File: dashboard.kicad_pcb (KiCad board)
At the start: 2 copper layers, 87.6 x 57.2 mm, 27 parts, among them J1 Conn_01x06, J2 Conn_01x04, J3 RJ45, J4 ESTOP, J5 776267-1, U1 MCP2515-xSO, U2 MCP2551-I-P, U3 LM317_SOT-223, U4 ILD74, Y1 16M

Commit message: Route PCB
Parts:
- removed A1: Arduino_Nano_v2.x, FBR_Footprints:Arduino_Nano_3D
- removed C1, C2: 27p, Capacitor_THT:C_Disc_D5.1mm_W3.2mm_P5.00mm
- removed C3: 0.1u, Capacitor_SMD:C_0603_1608Metric_Pad1.08x0.95mm_HandSolder
- removed C4: 1u, Capacitor_SMD:C_0603_1608Metric_Pad1.08x0.95mm_HandSolder
- removed J1: Conn_01x06, Connector_PinHeader_2.54mm:PinHeader_1x06_P2.54mm_Vertical
- removed R2: 20k, Resistor_THT:R_Axial_DIN0207_L6.3mm_D2.5mm_P7.62mm_Horizontal
- removed R3: 715, Resistor_SMD:R_0603_1608Metric_Pad0.98x0.95mm_HandSolder
- removed R4: 240, Resistor_SMD:R_0603_1608Metric_Pad0.98x0.95mm_HandSolder
- removed U1: MCP2515-xSO, Package_DIP:DIP-18_W7.62mm
- removed U3: LM317_SOT-223, Package_TO_SOT_SMD:SOT-223-3_TabPin2
- removed Y1: 16M, Crystal:Crystal_HC49-U_Vertical
- added C8: 10u, Capacitor_THT:C_Disc_D5.1mm_W3.2mm_P5.00mm, F.Cu at (122.5, 101.0)
- added C9: 10u, Capacitor_THT:C_Disc_D5.1mm_W3.2mm_P5.00mm, F.Cu at (108.5, 101.0)
- added L3: 12u, Inductor_SMD:L_Wuerth_WE-PD-Typ-7345, F.Cu at (115.5, 103.5)
- added Q1: 2N7002, Package_TO_SOT_THT:TO-92L_Inline_Wide, F.Cu at (116.5, 132.2)
- J2: value Conn_01x04 -> Conn_01x02; footprint Connector_PinHeader_2.54mm:PinHeader_1x04_P2.54mm_Vertical -> Connector_JST:JST_EH_B2B-EH-A_1x02_P2.50mm_Vertical
- J4: value ESTOP -> Conn_01x10; footprint Connector_PinHeader_2.54mm:PinHeader_1x02_P2.54mm_Vertical -> Connector_JST:JST_EH_B10B-EH-A_1x10_P2.50mm_Vertical
- R1: value 10k -> 120
- R6, R7: footprint Resistor_SMD:R_0603_1608Metric_Pad0.98x0.95mm_HandSolder -> Resistor_THT:R_Axial_DIN0207_L6.3mm_D2.5mm_P7.62mm_Horizontal
- U2: value MCP2551-I-P -> R-78C5.0-1.0; footprint Package_DIP:DIP-8_W7.62mm -> Converter_DCDC:Converter_DCDC_RECOM_R-78E-0.5_THT
- moved J4 81.4 mm to (180.5, 124.8), turned to 90 degrees
- moved U2 44.1 mm to (113.0, 96.5)
- moved R5 26.1 mm to (174.5, 123.2)
- moved U4 21.9 mm to (130.1, 138.5), turned to 180 degrees
- moved R6 19.3 mm to (122.5, 121.9)
- moved R7 18.2 mm to (122.5, 126.4)
- moved R1 14.1 mm to (110.4, 138.6), turned to 0 degrees
- moved J2 5.61 mm to (103.0, 112.5), turned to -90 degrees
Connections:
- J2 pad 1: +5V -> /Shutdown1
- J2 pad 2: /DISP_TX -> /Shutdown2
- J3 pad 2: +12V -> +5V
- J4 pad 1: /Shutdown1 -> /Neutral_LED+
- J4 pad 2: /Shutdown2 -> /Neutral
- J5 pad 12: GND -> /Spare_Switch_Sig
- U2 pad 1: /CAN_TX -> Net-(U2-IN)
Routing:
- net /SPI_CS: track 55.7 -> 0.00 mm
- net /SPI_MISO: track 53.7 -> 0.00 mm
- net +5V: track 187.4 -> 135.6 mm, vias 1 -> 0
- net /SPI_SCK: track 50.9 -> 0.00 mm, vias 1 -> 0
- net /SPI_MOSI: track 50.3 -> 0.00 mm
- net /Shift_Up: track 80.2 -> 44.0 mm
- net /Shutdown2: track 55.8 -> 91.1 mm, vias 0 -> 1
- net /Spare_Switch_Sig: track 0.00 -> 34.0 mm
- net /Shift_Dn: track 76.0 -> 42.2 mm
- net /CANH: track 61.8 -> 30.4 mm
- net /Shutdown1: track 51.1 -> 81.7 mm, vias 0 -> 1
- net /CANL: track 56.1 -> 28.9 mm
- net /DISP_TX: track 22.1 -> 0.00 mm
- net /DISP_RX: track 22.1 -> 0.00 mm
- net /CAN_TX: track 15.7 -> 0.00 mm
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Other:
- board text added: "+"
- board text added: "-"
- board text added: "Fan SW"
- board text added: "Neutral"
- board text added: "SW2"
- board text added: "Shtdwn"
- board text added: "Starter"
- board text removed: "5V"
- board text removed: "ESTOP"
- board text removed: "Fan SW - +"
- board text removed: "GND"
- board text removed: "Neutral - +"
- board text removed: "RX"
- board text removed: "Starter - +"
- board text removed: "TX"

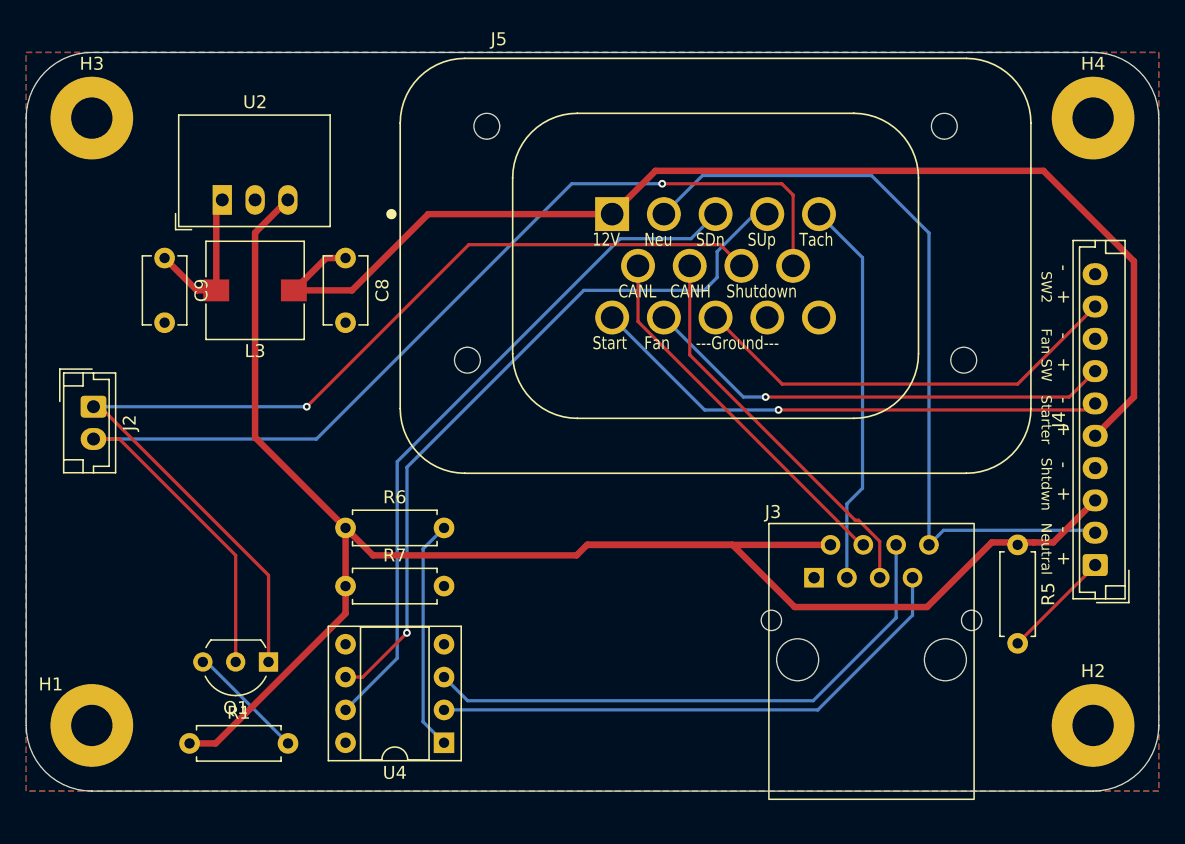
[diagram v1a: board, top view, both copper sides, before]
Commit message: Add both power supplies
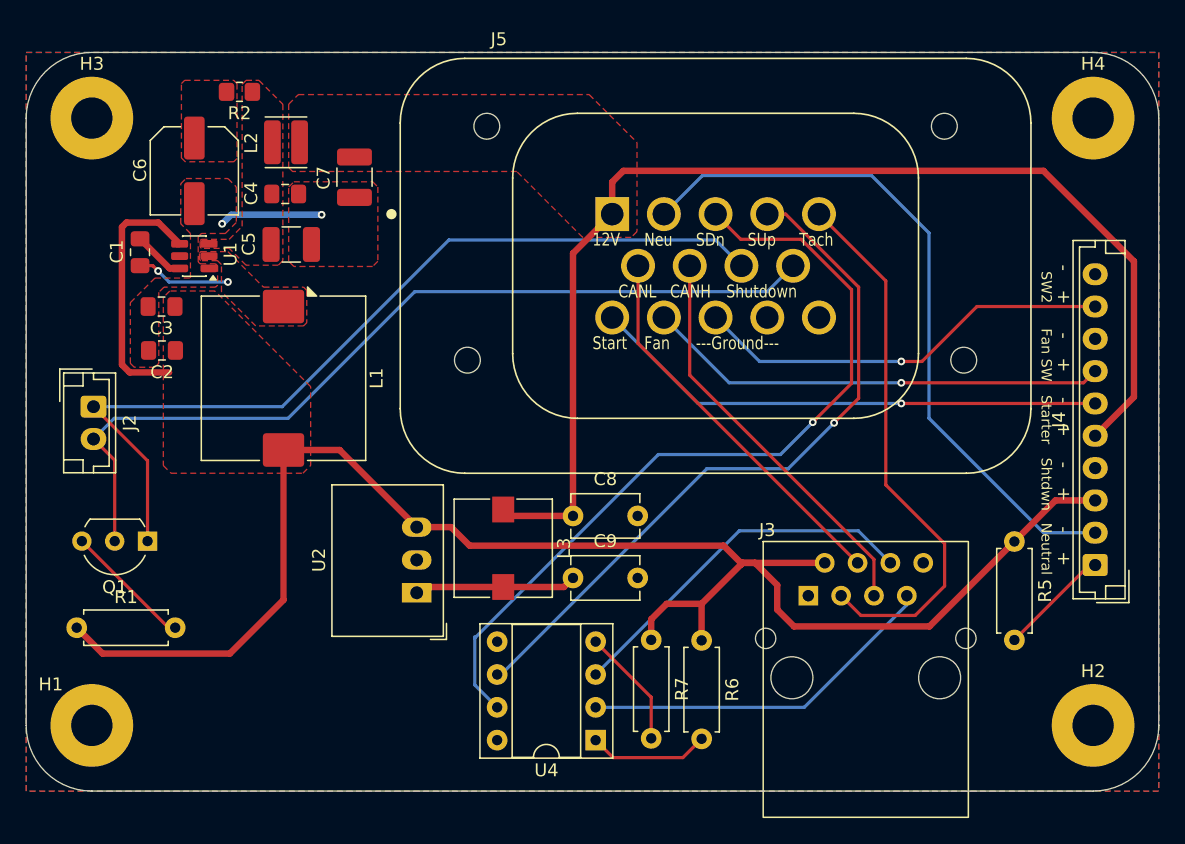
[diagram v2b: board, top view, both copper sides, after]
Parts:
- added C1: 100n, Capacitor_SMD:C_0805_2012Metric_Pad1.18x1.45mm_HandSolder, F.Cu at (106.6, 100.5)
- added C2: 22u, Capacitor_SMD:C_0805_2012Metric_Pad1.18x1.45mm_HandSolder, F.Cu at (108.3, 108.2)
- added C3: 100n, Capacitor_SMD:C_0805_2012Metric_Pad1.18x1.45mm_HandSolder, F.Cu at (108.3, 104.8)
- added C4: 100n, Capacitor_SMD:C_0805_2012Metric_Pad1.18x1.45mm_HandSolder, F.Cu at (117.8, 96.0)
- added C5: 22u, Capacitor_SMD:C_1210_3225Metric_Pad1.33x2.70mm_HandSolder, F.Cu at (118.3, 100.0)
- added C6: 56u, Capacitor_SMD:C_Elec_6.3x5.8, F.Cu at (110.8, 94.2)
- added C7: 10u, Capacitor_SMD:C_1210_3225Metric_Pad1.33x2.70mm_HandSolder, F.Cu at (123.2, 94.7)
- added L1: 15u, Inductor_SMD:L_TDK_SLF12575, F.Cu at (117.7, 110.3)
- added L2: 560n, Inductor_SMD:L_Wuerth_MAPI-3012, F.Cu at (117.9, 92.0)
- added R2: 100m, Resistor_SMD:R_0805_2012Metric_Pad1.20x1.40mm_HandSolder, F.Cu at (114.3, 88.1)
- added U1: TPS542025DDC, Package_TO_SOT_SMD:SOT-23-6, F.Cu at (110.8, 100.8)
- moved C9 40.1 mm to (140.1, 125.8), turned to 0 degrees
- moved U2 33.9 mm to (128.0, 126.9), turned to 90 degrees
- moved R6 28.9 mm to (150.1, 130.6), turned to -90 degrees
- moved L3 27.7 mm to (134.7, 123.5), turned to -90 degrees
- moved C8 26.6 mm to (140.1, 121.0), turned to 0 degrees
- moved R7 24.0 mm to (146.2, 130.5), turned to -90 degrees
- moved Q1 13.2 mm to (107.2, 122.9)
- moved R1 12.5 mm to (101.7, 129.6)
- moved U4 11.7 mm to (141.8, 138.3)
- moved J3 1.46 mm to (158.3, 127.1)
- moved R5 0.36 mm to (174.2, 122.9)
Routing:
- net /Shutdown2: track 91.1 -> 69.0 mm, vias 1 -> 0
- net /Shift_Up: track 44.0 -> 28.4 mm
- net /Shift_Dn: track 42.2 -> 28.1 mm
- net /Shutdown1: track 81.7 -> 68.4 mm, vias 1 -> 0
- net /Tacho: track 30.0 -> 42.4 mm
- net /Shift_Dn_Out: track 53.4 -> 63.7 mm, vias 0 -> 1
- net Net-(R7-Pad2): track 0.00 -> 9.26 mm
- net Net-(R6-Pad2): track 18.0 -> 9.36 mm
- net +5V: track 135.6 -> 143.6 mm
- net GND: track 0.00 -> 7.99 mm, vias 0 -> 2
- net Net-(U1-SW): track 0.00 -> 7.32 mm, vias 0 -> 2
- net /Neutral: track 61.1 -> 54.4 mm
- net Net-(U1-BOOT): track 0.00 -> 4.01 mm
- net /Spare_Switch_Sig: track 34.0 -> 32.5 mm, vias 0 -> 1
- net /CANL: track 28.9 -> 30.0 mm
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- added copper zone on F.Cu, net +12V
- added copper zone on F.Cu, net +5V
- added copper zone on F.Cu, net Net-(C6-Pad1)
- added copper zone on F.Cu, net Net-(U1-SW)
- added copper zone on F.Cu, net Net-(U1-VIN)

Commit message: Add power supply protection
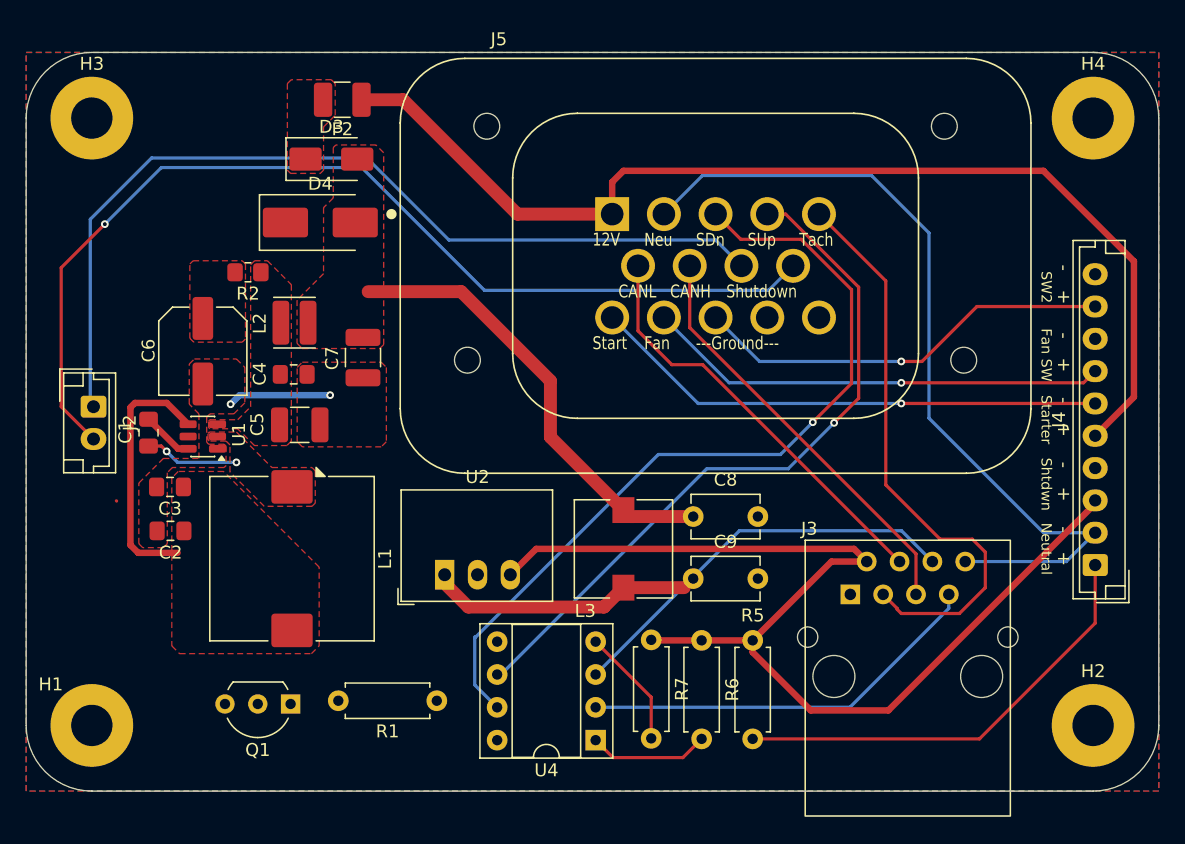
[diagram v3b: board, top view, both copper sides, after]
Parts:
- added D3: SS34, Diode_SMD:D_SMA, F.Cu at (121.4, 93.3)
- added D4: SMBJ24CA, Diode_SMD:D_SMB_Handsoldering, F.Cu at (120.5, 98.2)
- added F2: MF-USHTD75KX/24-2, Fuse:Fuse_1210_3225Metric_Pad1.42x2.65mm_HandSolder, F.Cu at (122.2, 88.8)
- moved R1 28.4 mm to (129.6, 135.2), turned to 180 degrees
- moved R5 21.6 mm to (154.0, 130.6)
- moved Q1 16.8 mm to (118.2, 135.5)
- moved C1 14.0 mm to (107.3, 114.5)
- moved C2 14.0 mm to (109.0, 122.1)
- moved C3 14.0 mm to (108.9, 118.7)
- moved C4 14.0 mm to (118.5, 110.0)
- moved C5 14.0 mm to (119.0, 113.9)
- moved C6 14.0 mm to (111.5, 108.2)
- moved C7 14.0 mm to (123.8, 108.7)
- moved L1 14.0 mm to (118.4, 124.3)
- moved L2 14.0 mm to (118.5, 106.0)
- moved R2 14.0 mm to (115.0, 102.1)
- moved U1 14.0 mm to (111.5, 114.8)
- moved C8 9.30 mm to (149.4, 121.0)
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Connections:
- C7 pad 1: +12V -> /PSU+
- C8 pad 1: +12V -> /PSU+
- L2 pad 1: +12V -> /PSU+
- L3 pad 1: +12V -> /PSU+
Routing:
- net +5V: track 143.6 -> 104.3 mm
- net /PSU+: track 0.00 -> 34.2 mm
- net /Neutral_LED+: track 8.65 -> 34.7 mm
- net /Neutral: track 54.4 -> 65.4 mm
- net /Shutdown2: track 69.0 -> 79.6 mm, vias 0 -> 1
- net Net-(Q1-D): track 10.00 -> 0.00 mm
- net Net-(U2-IN): track 12.9 -> 21.6 mm
- net +12V: track 91.1 -> 83.9 mm
- net /Shift_Dn: track 28.1 -> 31.6 mm
- net /Shift_Up: track 28.4 -> 31.6 mm
- net /Tacho: track 42.4 -> 45.1 mm
- net /CANL: track 30.0 -> 32.7 mm
- net /Shutdown1: track 68.4 -> 70.4 mm
- net /CANH: track 31.4 -> 32.7 mm
- added copper zone on F.Cu, net /PSU+
- added copper zone on F.Cu, net Net-(D3-K)
- removed copper zone on F.Cu, net +12V

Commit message: Revert "Add power supply protection"
This reverts commit 6c38df0548b9625adbd3b6c051cb9005b09ba150.
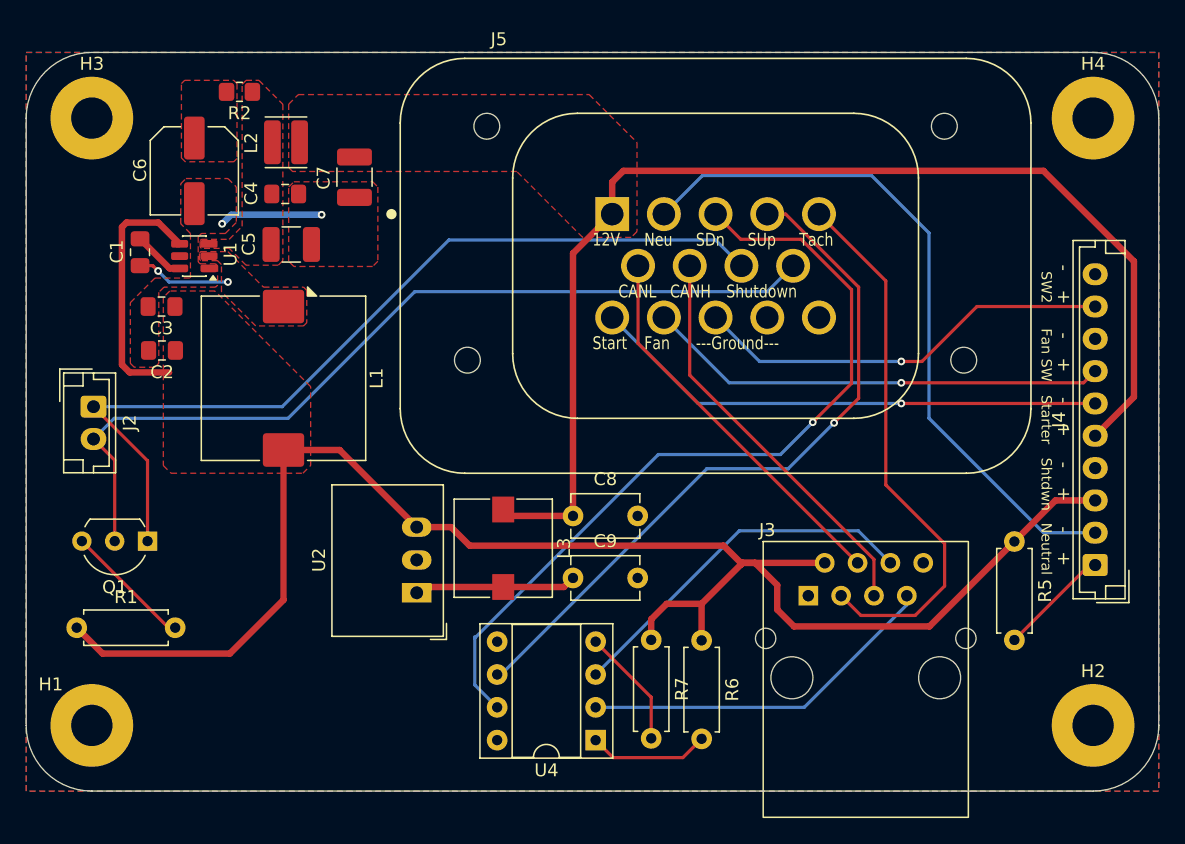
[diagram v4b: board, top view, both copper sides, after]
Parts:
- removed D3: SS34, Diode_SMD:D_SMA
- removed D4: SMBJ24CA, Diode_SMD:D_SMB_Handsoldering
- removed F2: MF-USHTD75KX/24-2, Fuse:Fuse_1210_3225Metric_Pad1.42x2.65mm_HandSolder
- moved R1 28.4 mm to (101.7, 129.6), turned to 0 degrees
- moved R5 21.6 mm to (174.2, 122.9)
- moved Q1 16.8 mm to (107.2, 122.9)
- moved C1 14.0 mm to (106.6, 100.5)
- moved C2 14.0 mm to (108.3, 108.2)
- moved C3 14.0 mm to (108.3, 104.8)
- moved C4 14.0 mm to (117.8, 96.0)
- moved C5 14.0 mm to (118.3, 100.0)
- moved C6 14.0 mm to (110.8, 94.2)
- moved C7 14.0 mm to (123.2, 94.7)
- moved L1 14.0 mm to (117.7, 110.3)
- moved L2 14.0 mm to (117.9, 92.0)
- moved R2 14.0 mm to (114.3, 88.1)
- moved U1 14.0 mm to (110.8, 100.8)
- moved C8 9.30 mm to (140.1, 121.0)
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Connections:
- C7 pad 1: /PSU+ -> +12V
- C8 pad 1: /PSU+ -> +12V
- L2 pad 1: /PSU+ -> +12V
- L3 pad 1: /PSU+ -> +12V
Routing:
- net +5V: track 104.3 -> 143.6 mm
- net /PSU+: track 34.2 -> 0.00 mm
- net /Neutral_LED+: track 34.7 -> 8.65 mm
- net /Neutral: track 65.4 -> 54.4 mm
- net /Shutdown2: track 79.6 -> 69.0 mm, vias 1 -> 0
- net Net-(Q1-D): track 0.00 -> 10.00 mm
- net Net-(U2-IN): track 21.6 -> 12.9 mm
- net +12V: track 83.9 -> 91.1 mm
- net /Shift_Dn: track 31.6 -> 28.1 mm
- net /Shift_Up: track 31.6 -> 28.4 mm
- net /Tacho: track 45.1 -> 42.4 mm
- net /CANL: track 32.7 -> 30.0 mm
- net /Shutdown1: track 70.4 -> 68.4 mm
- net /CANH: track 32.7 -> 31.4 mm
- added copper zone on F.Cu, net +12V
- removed copper zone on F.Cu, net /PSU+
- removed copper zone on F.Cu, net Net-(D3-K)

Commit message: added protection for switching regulator, rerouted PCB
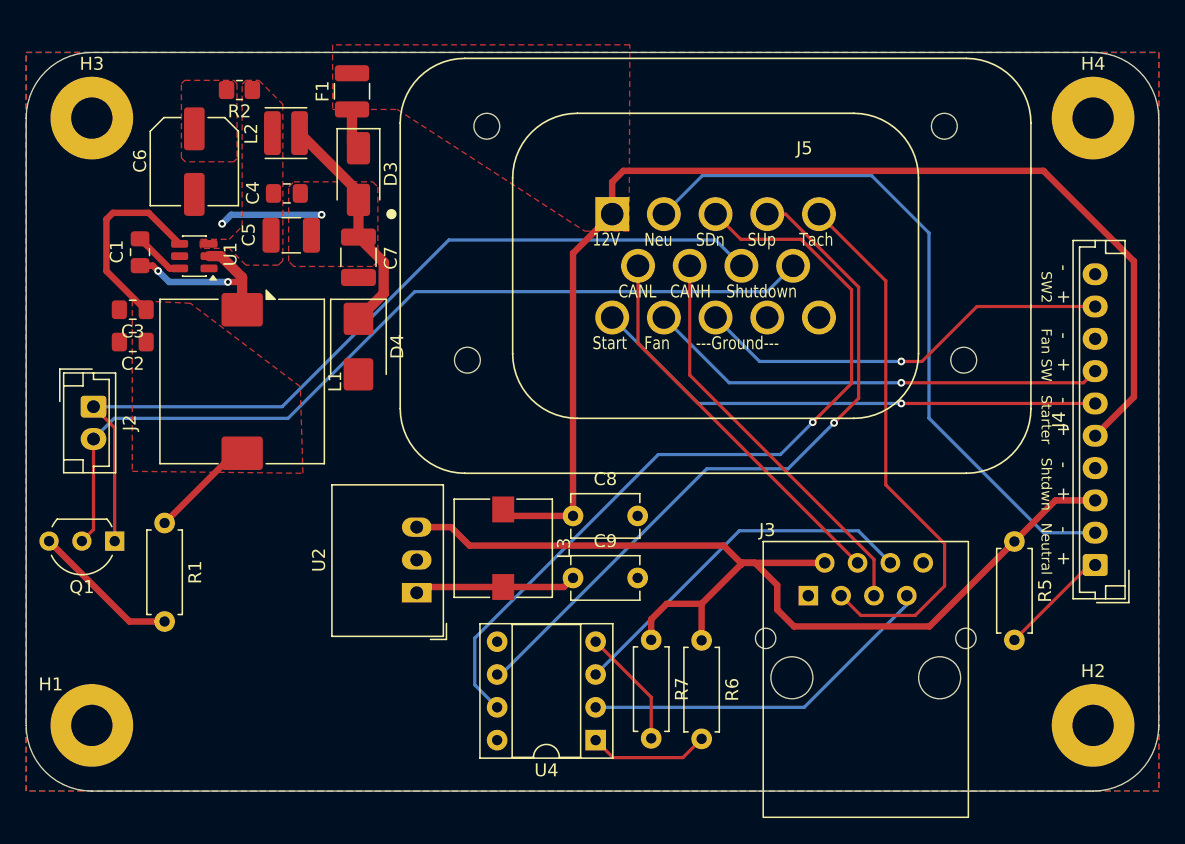
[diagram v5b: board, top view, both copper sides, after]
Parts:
- added D3: SS34, Diode_SMD:D_SMA, F.Cu at (123.5, 94.5)
- added D4: SMBJ24CA, Diode_SMD:D_SMB, F.Cu at (123.5, 107.8)
- added F1: MF-USHT075KX/24-2, Inductor_SMD:L_1210_3225Metric, F.Cu at (123.0, 88.1)
- moved R1 10.6 mm to (108.5, 121.5), turned to -90 degrees
- moved C7 6.20 mm to (123.5, 100.9)
- moved L1 3.21 mm to (114.5, 110.5)
- moved Q1 2.54 mm to (104.6, 122.9)
- moved C2 2.35 mm to (106.0, 107.5)
- moved C3 2.24 mm to (106.0, 105.0)
- moved C5 0.71 mm to (118.3, 99.2)
- moved C6 0.71 mm to (110.8, 93.5)
- moved L2 0.71 mm to (117.9, 91.3)
- moved R2 0.14 mm to (114.3, 88.0)
- moved C4 0.14 mm to (118.0, 96.0)
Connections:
- C7 pad 1: +12V -> Net-(D3-A)
- L2 pad 1: +12V -> Net-(D3-A)
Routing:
- net +5V: track 143.6 -> 104.0 mm
- net Net-(D3-A): track 0.00 -> 18.7 mm
- net Net-(U1-SW): track 7.32 -> 14.3 mm
- net Net-(D3-K): track 0.00 -> 3.21 mm
- net Net-(Q1-D): track 10.00 -> 11.7 mm
- net /Shutdown2: track 69.0 -> 68.0 mm
- net /Shutdown1: track 68.4 -> 67.4 mm
- net /Shift_Up_Out: track 56.5 -> 55.5 mm
- net /Starter_Sig: track 40.8 -> 40.1 mm
- removed copper zone on F.Cu, net Net-(U1-SW)

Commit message: Add power supply protection
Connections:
- C7 pad 1: Net-(D3-A) -> /PSU+
- C8 pad 1: +12V -> /PSU+
- D3 pad 2: Net-(D3-A) -> /PSU+
- D4 pad 1: Net-(D3-A) -> /PSU+
- L2 pad 1: Net-(D3-A) -> /PSU+
- L3 pad 1: +12V -> /PSU+
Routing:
- net /PSU+: track 0.00 -> 57.2 mm
- net +12V: track 91.1 -> 60.9 mm
- net Net-(D3-A): track 18.7 -> 0.00 mm
- net +5V: track 104.0 -> 119.9 mm

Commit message: Add text and labels
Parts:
- removed G***: LOGO, FBR_Footprints:FBR_Logo_.9in
- added Dashboard (2026): LOGO, Dashboard:FBR_Logo_.9in, B.Cu at (117.6, 100.6)
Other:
- board text added: "Right E-Stop"
- board text removed: "Designed by Oliver Gaskell, January 2025"

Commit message: Fix DRC errors
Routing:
- net /Neutral: track 54.4 -> 64.1 mm
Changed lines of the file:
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@@
+	)
+	(segment
+		(start 170.578 121.2)
+		(end 175.45 121.2)
+		(width 0.25)
+		(layer "B.Cu")
+		(net 8)
 	)
 	(segment
@@
 	)
 	(segment
+		(start 167.195 124.583)
+		(end 170.578 121.2)
+		(width 0.25)
+		(layer "B.Cu")
+		(net 8)
+	)
+	(segment
 		(start 176.5 122.25)
+		(end 175.45 121.2)
+		(width 0.25)
+		(layer "B.Cu")
+		(net 8)
+	)
+	(segment
+		(start 175.45 121.2)
 		(end 167.64 113.39)
 		(width 0.25)
